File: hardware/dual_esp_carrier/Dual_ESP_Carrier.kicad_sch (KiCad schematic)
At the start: 0 parts

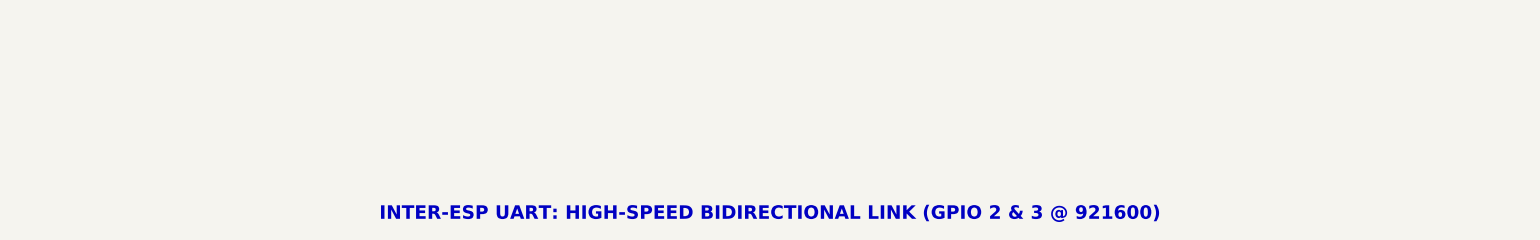
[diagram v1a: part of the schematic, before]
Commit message: feat: enhance battery monitoring web UI with dynamic cell configurations and capacity controls
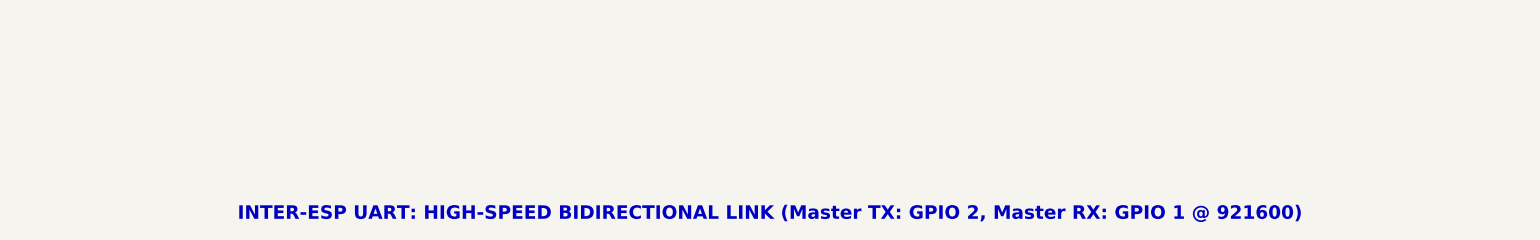
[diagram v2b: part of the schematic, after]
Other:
- note added: "INTER-ESP UART: HIGH-SPEED BIDIRECTIONAL LINK (Master TX: GPIO 2, Master RX: GPIO 1 @ 921600)"
- note removed: "INTER-ESP UART: HIGH-SPEED BIDIRECTIONAL LINK (GPIO 2 & 3 @ 921600)"
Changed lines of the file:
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@@
 		)
 	)
-	(text "INTER-ESP UART: HIGH-SPEED BIDIRECTIONAL LINK (GPIO 2 & 3 @ 921600)"
+	(text "INTER-ESP UART: HIGH-SPEED BIDIRECTIONAL LINK (Master TX: GPIO 2, Master RX: GPIO 1 @ 921600)"
 		(exclude_from_sim no)
 		(at 100 80 0)

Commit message: feat: update Dual ESP carrier PCB layout, gerbers, and pinout documentation
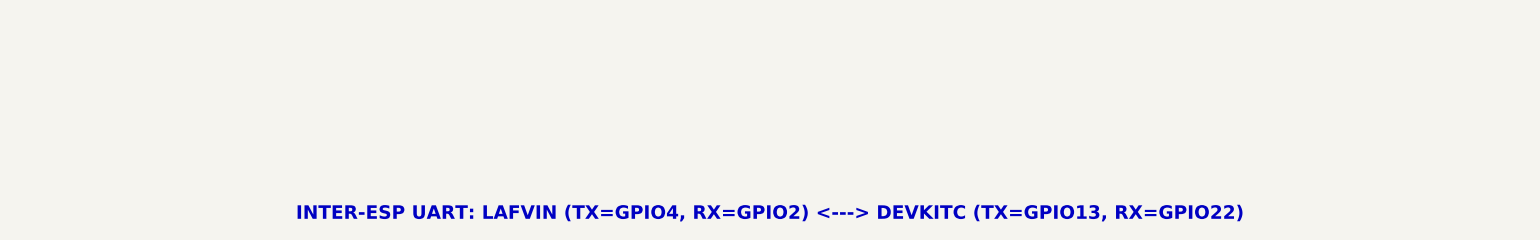
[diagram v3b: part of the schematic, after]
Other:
- note added: "INTER-ESP UART: LAFVIN (TX=GPIO4, RX=GPIO2) <---> DEVKITC (TX=GPIO13, RX=GPIO22)"
- note removed: "INTER-ESP UART: HIGH-SPEED BIDIRECTIONAL LINK (Master TX: GPIO 2, Master RX: GPIO 1 @ 921600)"
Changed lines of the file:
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@@
 		)
 	)
-	(text "INTER-ESP UART: HIGH-SPEED BIDIRECTIONAL LINK (Master TX: GPIO 2, Master RX: GPIO 1 @ 921600)"
+	(text "INTER-ESP UART: LAFVIN (TX=GPIO4, RX=GPIO2) <---> DEVKITC (TX=GPIO13, RX=GPIO22)"
 		(exclude_from_sim no)
 		(at 100 80 0)
